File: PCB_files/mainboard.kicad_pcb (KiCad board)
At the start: 2 copper layers, 95.2 x 55.9 mm, 48 parts, among them J1 Conn_01x01_Male, J2 Conn_01x01_Male, J3 Conn_01x01_Male, J4 Conn_01x20, J5 Conn_01x20, J6 Conn_01x06_Male, U1 IFX007TAUMA1, U2 IFX007TAUMA1, U3 IFX007TAUMA1, U4 LM2931-5.0_SO8

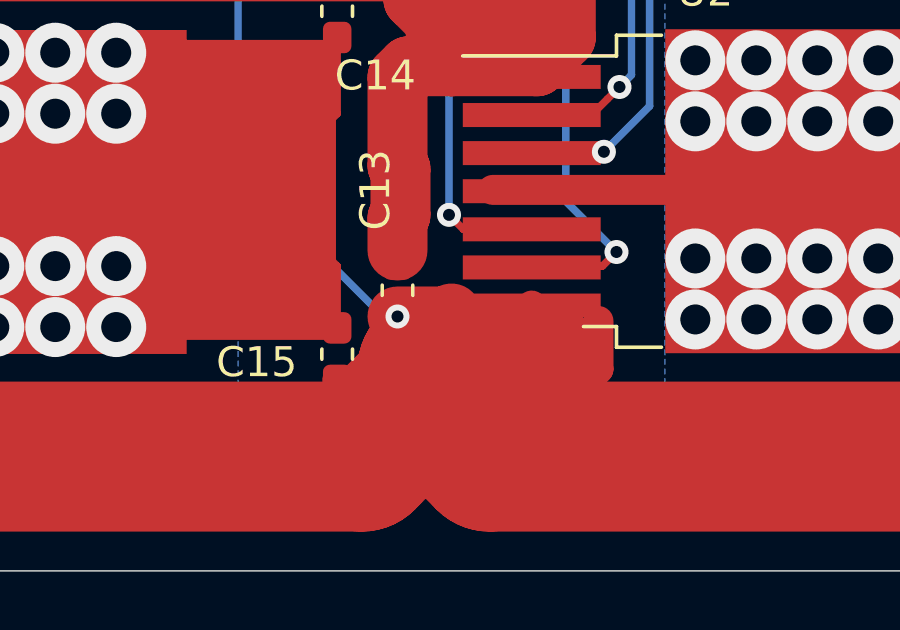
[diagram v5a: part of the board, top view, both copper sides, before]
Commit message: Minor PCB fixes + added gerber and drill files (in zip)
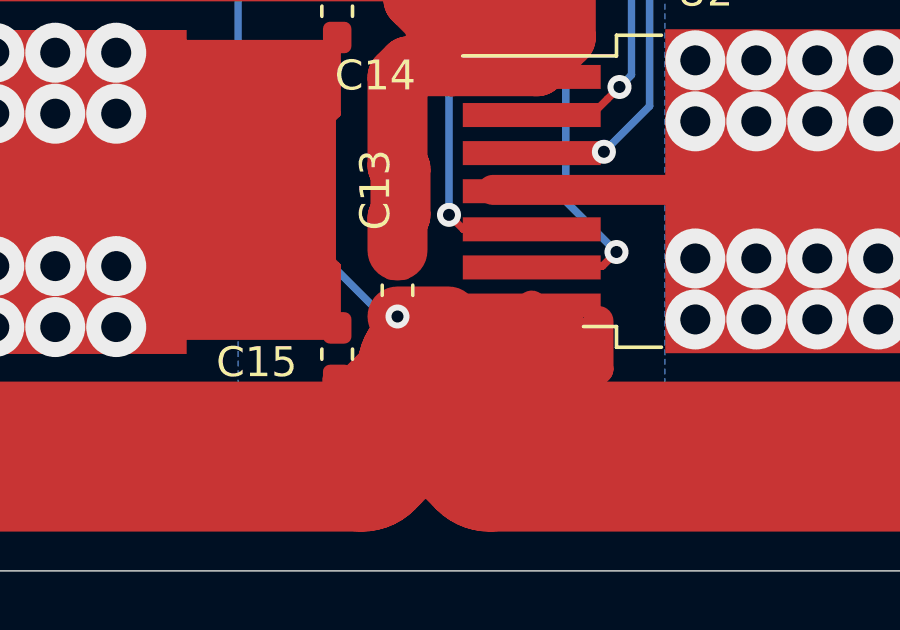
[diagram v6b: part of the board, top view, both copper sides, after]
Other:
- board text added: "RobESC V1.0 AHP Industries 10/2020"
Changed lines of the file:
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@@
   (general
     (thickness 1.6)
-    (drawings 15)
-    (tracks 396)
+    (drawings 16)
+    (tracks 395)
     (zones 0)
     (modules 48)
@@
   (page A4)
   (layers
-    (0 F.Cu signal)
+    (0 F.Cu signal hide)
     (31 B.Cu signal)
-    (32 B.Adhes user)
-    (33 F.Adhes user)
+    (32 B.Adhes user hide)
+    (33 F.Adhes user hide)
     (34 B.Paste user)
-    (35 F.Paste user)
+    (35 F.Paste user hide)
     (36 B.SilkS user)
-    (37 F.SilkS user)
+    (37 F.SilkS user hide)
     (38 B.Mask user)
-    (39 F.Mask user)
-    (40 Dwgs.User user)
-    (41 Cmts.User user)
-    (42 Eco1.User user)
-    (43 Eco2.User user)
+    (39 F.Mask user hide)
+    (40 Dwgs.User user hide)
+    (41 Cmts.User user hide)
+    (42 Eco1.User user hide)
+    (43 Eco2.User user hide)
     (44 Edge.Cuts user)
-    (45 Margin user)
+    (45 Margin user hide)
     (46 B.CrtYd user)
-    (47 F.CrtYd user)
+    (47 F.CrtYd user hide)
     (48 B.Fab user)
-    (49 F.Fab user)
+    (49 F.Fab user hide)
   )
   (setup
@@
     (visible_elements 7FFFFFFF)
     (pcbplotparams
-      (layerselection 0x010fc_ffffffff)
+      (layerselection 0x010f0_ffffffff)
       (usegerberextensions false)
       (usegerberattributes true)
@@
       (drillshape 0)
       (scaleselection 1)
-      (outputdirectory ""))
+      (outputdirectory "./"))
   )
   (net 0 "")
@@
     )
   )
+  (gr_text "RobESC V1.0   AHP Industries 10/2020" (at 185.42 73.66) (layer B.SilkS)
+    (effects (font (size 2 1.5) (thickness 0.15)) (justify mirror))
+  )
   (gr_text 1 (at 149.67712 75.26528) (layer F.SilkS)
     (effects (font (size 1 1) (thickness 0.15)))
@@
   (segment (start 164.08 106.68) (end 165.1 106.68) (width 0.25) (layer F.Cu) (net 38))
   (segment (start 129.54 105.41) (end 129.54 105.335) (width 2) (layer F.Cu) (net 38))
-  (segment (start 165.000601 104.55) (end 165.1 104.450601) (width 2) (layer F.Cu) (net 38))
   (segment (start 163.3 104.55) (end 165.000601 104.55) (width 2) (layer F.Cu) (net 38))
   (segment (start 191.77 106.68) (end 191.77 106.67) (width 2) (layer F.Cu) (net 38))
